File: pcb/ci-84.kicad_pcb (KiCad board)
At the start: 2 copper layers, 91 x 217 mm, 117 parts, among them J1 Conn_01x02, SW1 SW_Push, SW10 XT0N, SW11 STAT, SW12 MATH, SW13 APPS, SW14 PRGM, SW15 VARS, SW16 CLEAR, SW17 X^-1, SW18 SIN, SW19 COS, SW2 Y=, SW20 TAN, SW21 ^, SW22 X^2, SW23 ,, SW24 (, SW25 ), SW26 DIVIDE, SW27 LOG, SW28 7, SW29 8, SW3 WINDOW, SW30 9, SW31 MULITPLY, SW32 IN, SW33 4, SW34 5, SW35 6, SW36 SUBTRACT, SW37 STO, SW38 1, SW39 2, SW4 ZOOM, SW40 3, SW41 ADD, SW42 ON, SW43 0, SW44 ., SW45 (-), SW46 ENTER, SW47 GRAPH, SW48 UP, SW49 RIGHT, SW5 TRACE, SW50 DOWN, SW51 LEFT, SW6 2ND, SW7 MODE, SW8 DEL, SW9 ALPHA, U1 STM32L471RGTx, U3 TPS63900, U4 TFT_320x240

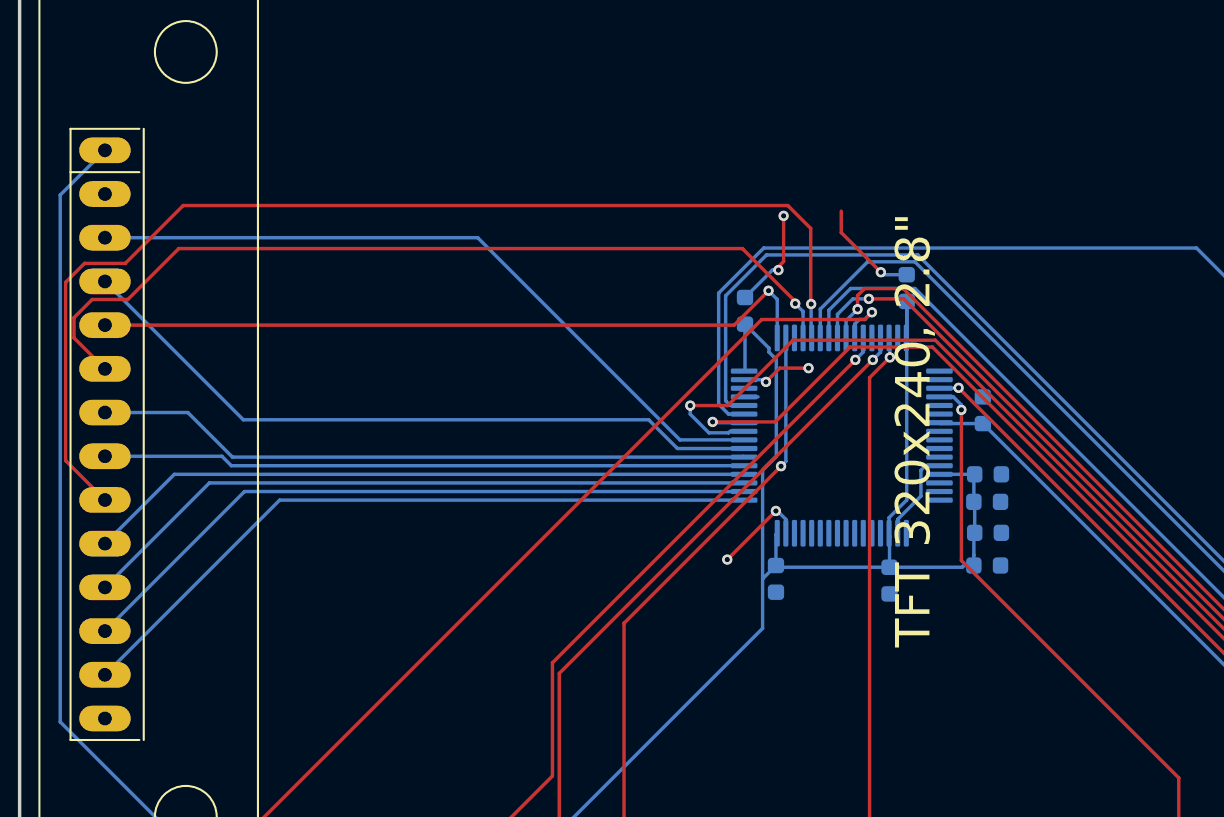
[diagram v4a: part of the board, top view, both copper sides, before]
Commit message: sw pins
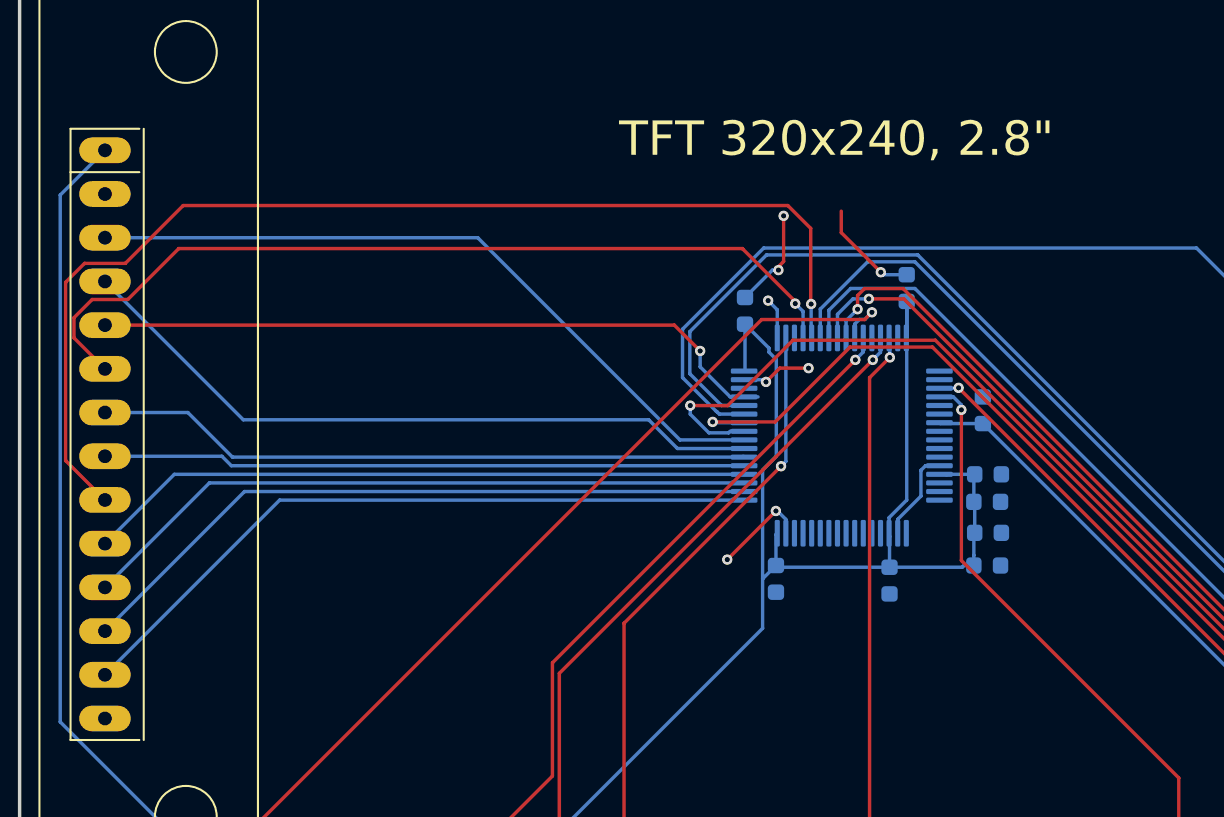
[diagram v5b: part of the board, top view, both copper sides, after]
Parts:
- J1: value Conn_01x02 -> jst-battery
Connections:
- U1 pad 45: unconnected-(U1-PA12-Pad45) -> /IO_DC
- U1 pad 46: unconnected-(U1-PA13-Pad46) -> /SWDIO
- U1 pad 49: /IO_DC -> /SWCLK
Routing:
- net /SWCLK: track 0.00 -> 2.39 mm, vias 0 -> 1
- net /IO_DC: track 42.3 -> 40.2 mm
- net /r5: track 235.4 -> 237.5 mm
- net /r4: track 212.7 -> 214.7 mm
- net unconnected-(U1-PA12-Pad45): track 0.81 -> 0.00 mm
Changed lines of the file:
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@@
 	(net 99 "/c4")
 	(net 100 "/c5")
-	(net 101 "unconnected-(U1-PA13-Pad46)")
-	(net 102 "unconnected-(U1-PA12-Pad45)")
+	(net 101 "/SWCLK")
+	(net 102 "/SWDIO")
 	(net 103 "unconnected-(U1-PC10-Pad51)")
 	(net 104 "unconnected-(U1-PA5-Pad21)")
@@
 		)
 		(fp_text user "TFT 320x240, 2.8\""
-			(at -0.254 -46.99 90)
+			(at -17.175 -42.515 180)
 			(layer "F.SilkS")
 			(effects
@@
 			)
 		)
-		(property "Value" "Conn_01x02"
+		(property "Value" "jst-battery"
 			(at 1 -4 0)
 			(layer "B.Fab")
@@
 			(layers "B.Cu" "B.Paste" "B.Mask")
 			(roundrect_rratio 0.25)
-			(net 102 "unconnected-(U1-PA12-Pad45)")
+			(net 8 "/IO_DC")
 			(pinfunction "PA12")
 			(pintype "bidirectional")
@@
 			(layers "B.Cu" "B.Paste" "B.Mask")
 			(roundrect_rratio 0.25)
-			(net 101 "unconnected-(U1-PA13-Pad46)")
+			(net 102 "/SWDIO")
 			(pinfunction "PA13")
 			(pintype "bidirectional")
@@
 			(layers "B.Cu" "B.Paste" "B.Mask")
 			(roundrect_rratio 0.25)
-			(net 8 "/IO_DC")
+			(net 101 "/SWCLK")
 			(pinfunction "PA14")
 			(pintype "bidirectional")
@@
 	)
 	(segment
-		(start 279.025 112.85)
+		(start 275.55 112.85)
 		(end 242.46 112.85)
 		(width 0.2)
@@
 	)
 	(segment
-		(start 281.025 110.85)
-		(end 279.025 112.85)
+		(start 277.05 114.35)
+		(end 275.55 112.85)
 		(width 0.2)
 		(layer "F.Cu")
@@
 	)
 	(via
-		(at 281.025 110.85)
+		(at 277.05 114.35)
 		(size 0.6)
 		(drill 0.3)
@@
 	)
 	(segment
-		(start 281.53 111.355)
-		(end 281.025 110.85)
+		(start 277.05 115.27241)
+		(end 278.79759 117.02)
 		(width 0.2)
 		(layer "B.Cu")
@@
 	)
 	(segment
-		(start 281.53 113.595)
-		(end 281.53 111.355)
+		(start 277.05 114.35)
+		(end 277.05 115.27241)
+		(width 0.2)
+		(layer "B.Cu")
+		(net 8)
+	)
+	(segment
+		(start 279.605 117.02)
+		(end 280.41241 117.02)
+		(width 0.2)
+		(layer "B.Cu")
+		(net 8)
+	)
+	(segment
+		(start 278.79759 117.02)
+		(end 279.605 117.02)
 		(width 0.2)
 		(layer "B.Cu")
@@
 	)
 	(segment
-		(start 289.694382 108.77)
-		(end 280.906304 108.77)
+		(start 280.906304 108.77)
+		(end 276.45 113.226304)
 		(width 0.2)
 		(layer "B.Cu")
@@
 	)
 	(segment
-		(start 280.906304 108.77)
-		(end 278.53 111.146304)
+		(start 276.45 113.226304)
+		(end 276.45 115.675)
 		(width 0.2)
 		(layer "B.Cu")
@@
 	)
 	(segment
-		(start 305.248529 201.95)
-		(end 316.6493 190.549229)
+		(start 316.6493 135.724918)
+		(end 289.694382 108.77)
 		(width 0.2)
 		(layer "B.Cu")
@@
 	)
 	(segment
-		(start 300.75 201.95)
-		(end 300.875 201.95)
+		(start 316.6493 190.549229)
+		(end 316.6493 135.724918)
 		(width 0.2)
 		(layer "B.Cu")
@@
 	)
 	(segment
-		(start 278.53 117.25241)
-		(end 278.79759 117.52)
+		(start 276.45 115.675)
+		(end 278.295 117.52)
 		(width 0.2)
 		(layer "B.Cu")
@@
 	)
 	(segment
-		(start 278.53 111.146304)
-		(end 278.53 117.25241)
+		(start 278.295 117.52)
+		(end 279.605 117.52)
 		(width 0.2)
 		(layer "B.Cu")
@@
 	)
 	(segment
-		(start 278.79759 117.52)
-		(end 279.605 117.52)
+		(start 305.248529 201.95)
+		(end 316.6493 190.549229)
 		(width 0.2)
 		(layer "B.Cu")
@@
 	)
 	(segment
-		(start 316.6493 190.549229)
-		(end 316.6493 135.724918)
+		(start 300.75 201.95)
+		(end 300.875 201.95)
 		(width 0.2)
 		(layer "B.Cu")
@@
 	)
 	(segment
-		(start 316.6493 135.724918)
-		(end 289.694382 108.77)
+		(start 289.694382 108.77)
+		(end 280.906304 108.77)
 		(width 0.2)
 		(layer "B.Cu")
@@
 	)
 	(segment
-		(start 278.69759 118.02)
+		(start 280.740618 108.37)
+		(end 276.025 113.085618)
+		(width 0.2)
+		(layer "B.Cu")
+		(net 45)
+	)
+	(segment
+		(start 278.168529 118.02)
 		(end 279.605 118.02)
 		(width 0.2)
@@
 	)
 	(segment
-		(start 278.125 110.985618)
-		(end 278.125 117.44741)
+		(start 305.895 108.37)
+		(end 280.740618 108.37)
 		(width 0.2)
 		(layer "B.Cu")
@@
 	)
 	(segment
-		(start 280.740618 108.37)
-		(end 278.125 110.985618)
+		(start 317.0493 191.4507)
+		(end 317.0493 119.5243)
 		(width 0.2)
 		(layer "B.Cu")
@@
 	)
 	(segment
-		(start 305.895 108.37)
-		(end 280.740618 108.37)
+		(start 317.0493 119.5243)
+		(end 305.895 108.37)
 		(width 0.2)
 		(layer "B.Cu")
@@
 	)
 	(segment
-		(start 301.125 207.375)
-		(end 317.0493 191.4507)
+		(start 278 117.875)
+		(end 278.023529 117.875)
 		(width 0.2)
 		(layer "B.Cu")
@@
 	)
 	(segment
-		(start 278.125 117.44741)
-		(end 278.69759 118.02)
+		(start 276.025 115.9)
+		(end 278 117.875)
 		(width 0.2)
 		(layer "B.Cu")
@@
 	)
 	(segment
-		(start 317.0493 191.4507)
-		(end 317.0493 119.5243)
+		(start 301.125 207.375)
+		(end 317.0493 191.4507)
 		(width 0.2)
 		(layer "B.Cu")
@@
 	)
 	(segment
-		(start 317.0493 119.5243)
-		(end 305.895 108.37)
+		(start 276.025 113.085618)
+		(end 276.025 115.9)
+		(width 0.2)
+		(layer "B.Cu")
+		(net 45)
+	)
+	(segment
+		(start 278.023529 117.875)
+		(end 278.168529 118.02)
 		(width 0.2)
 		(layer "B.Cu")
@@
 		(net 100)
 	)
+	(via
+		(at 281 111.425)
+		(size 0.6)
+		(drill 0.3)
+		(layers "F.Cu" "B.Cu")
+		(net 101)
+	)
 	(segment
-		(start 279.605 117.02)
-		(end 280.41241 117.02)
+		(start 281.53 113.595)
+		(end 281.53 111.955)
+		(width 0.2)
+		(layer "B.Cu")
+		(net 101)
+	)
+	(segment
+		(start 281.53 111.955)
+		(end 281 111.425)
 		(width 0.2)
 		(layer "B.Cu")
-		(net 102)
+		(net 101)
 	)
 	(segment

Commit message: swd
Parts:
- added J2: SWD, Connector_PinHeader_2.54mm:PinHeader_1x04_P2.54mm_Vertical, B.Cu at (275.7, 146.9)
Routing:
- net /SWCLK: track 2.39 -> 49.5 mm, vias 1 -> 3
- net /SWDIO: track 0.00 -> 44.0 mm, vias 0 -> 3
- net VDD: track 157.4 -> 170.0 mm
- net /r7: track 381.5 -> 380.3 mm
